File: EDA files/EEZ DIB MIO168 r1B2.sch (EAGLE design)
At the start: 295 parts, among them IC1 M24C32-WMN6P, IC10 DAC7760IPWPR, IC11 DAC7760IPWPR, IC12 OPA376AIDBVR, IC13 DAC7563TDGSR, IC14 OPA2196IDR, IC15 BTS3408G, IC16 BTS3408G, IC17 BTS3408G, IC18 BTS3408G, IC19 74HC126PW,118, IC2 Si8641BB-B-IS1, IC20 TL431B, IC21 DG468DV-T1-E3, IC22 DG468DV-T1-E3, IC23 DG468DV-T1-E3, IC24 DG468DV-T1-E3, IC25 DG468DV-T1-E3, IC26 DG468DV-T1-E3, IC27 DG468DV-T1-E3, IC28 DG468DV-T1-E3, IC29 DG468DV-T1-E3, IC3 Si8641BB-B-IS1, IC30 DG468DV-T1-E3, IC31 DG468DV-T1-E3, IC32 DG468DV-T1-E3, IC33 DG468DV-T1-E3, IC34 DG468DV-T1-E3, IC35 OPA376AIDBVR, IC36 ADS8674IDBT, IC4 L78L12, IC5 LP2985-50DBVR, IC6 LP2985-33DBVR, IC7 L79L12, IC8 STM32F446ZCT6, IC9 OPA2196IDR, J1 4907, J2 503398-1892, Q1 2N7002PS,115, Q10 BSS169, Q11 BSS169, Q12 BSS169, Q13 BSS169, Q2 2N7002PS,115, Q3 2N7002PS,115, Q4 2N7002PS,115, Q5 2N7002PS,115, Q6 BSS169, Q7 BSS169, Q8 BSS169, Q9 BSS169, X1 77317-104-28LF, X2 SSW-106-02-S-S, X3 691327310016, X4 691327310016, Y1 25MHz

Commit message: #1 fixed
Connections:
- net GND: now also IC12P.V-; no longer IC12P.V+
- net N$71: now also IC12P.V+; no longer IC12P.V-
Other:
- moved on the sheet: IC12P
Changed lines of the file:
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@@
 <setting verticaltext="up"/>
 </settings>
-<grid distance="0.1" unitdist="inch" unit="inch" style="lines" multiple="1" display="no" altdistance="0.01" altunitdist="inch" altunit="inch"/>
+<grid distance="0.025" unitdist="inch" unit="inch" style="lines" multiple="4" display="no" altdistance="0.01" altunitdist="inch" altunit="inch"/>
 <layers>
 <layer number="1" name="Top" color="4" fill="1" visible="no" active="no"/>
@@
 <layer number="111" name="111" color="7" fill="1" visible="no" active="no"/>
 <layer number="112" name="tSilk" color="7" fill="1" visible="no" active="no"/>
-<layer number="113" name="ReferenceLS" color="7" fill="1" visible="yes" active="yes"/>
-<layer number="114" name="EEZ" color="12" fill="1" visible="yes" active="yes"/>
-<layer number="115" name="CH1" color="13" fill="1" visible="yes" active="yes"/>
 <layer number="116" name="Patch_BOT" color="7" fill="1" visible="no" active="no"/>
-<layer number="117" name="CH2" color="9" fill="1" visible="yes" active="yes"/>
 <layer number="118" name="Rect_Pads" color="7" fill="1" visible="no" active="no"/>
-<layer number="119" name="CH3" color="12" fill="1" visible="yes" active="yes"/>
 <layer number="120" name="lotbs" color="7" fill="1" visible="no" active="no"/>
 <layer number="121" name="_tsilk" color="7" fill="1" visible="no" active="no"/>
@@
 <layer number="127" name="_tValues" color="7" fill="1" visible="no" active="no"/>
 <layer number="128" name="_bValues" color="7" fill="1" visible="no" active="no"/>
-<layer number="129" name="sram_cmd" color="13" fill="1" visible="yes" active="yes"/>
-<layer number="130" name="sram_ctrl" color="2" fill="1" visible="yes" active="yes"/>
 <layer number="131" name="tAdjust" color="7" fill="1" visible="no" active="no"/>
 <layer number="132" name="bAdjust" color="7" fill="1" visible="no" active="no"/>
@@
 <attribute name="VALUE" x="100.33" y="158.75" size="1.778" layer="96" rot="MR180"/>
 </instance>
-<instance part="IC12" gate="P" x="86.36" y="119.38" smashed="yes" rot="MR180">
-<attribute name="NAME" x="83.185" y="120.65" size="1.778" layer="95" rot="MR180"/>
-</instance>
 <instance part="FB4" gate="G$1" x="93.98" y="137.16" smashed="yes">
 <attribute name="NAME" x="92.075" y="138.5316" size="1.778" layer="95"/>
@@
 <attribute name="VALUE" x="121.92" y="11.938" size="1.778" layer="96"/>
 </instance>
+<instance part="IC12" gate="P" x="86.36" y="119.38" smashed="yes">
+<attribute name="NAME" x="83.185" y="118.745" size="1.778" layer="95"/>
+</instance>
 </instances>
 <busses>
@@
 </segment>
 <segment>
-<pinref part="IC12" gate="P" pin="V+"/>
 <pinref part="SUPPLY31" gate="GND" pin="GND"/>
 <wire x1="86.36" y1="109.22" x2="86.36" y2="111.76" width="0.1524" layer="91"/>
@@
 <wire x1="86.36" y1="111.76" x2="93.98" y2="111.76" width="0.1524" layer="91"/>
 <wire x1="93.98" y1="111.76" x2="93.98" y2="116.84" width="0.1524" layer="91"/>
+<pinref part="IC12" gate="P" pin="V-"/>
 <junction x="86.36" y="111.76"/>
 </segment>
@@
 <pinref part="FB4" gate="G$1" pin="1"/>
 <wire x1="88.9" y1="137.16" x2="86.36" y2="137.16" width="0.1524" layer="91"/>
-<pinref part="IC12" gate="P" pin="V-"/>
 <wire x1="86.36" y1="137.16" x2="76.2" y2="137.16" width="0.1524" layer="91"/>
 <wire x1="86.36" y1="127" x2="86.36" y2="137.16" width="0.1524" layer="91"/>
@@
 <wire x1="86.36" y1="127" x2="93.98" y2="127" width="0.1524" layer="91"/>
 <wire x1="93.98" y1="127" x2="93.98" y2="124.46" width="0.1524" layer="91"/>
+<pinref part="IC12" gate="P" pin="V+"/>
 <junction x="86.36" y="127"/>
 </segment>

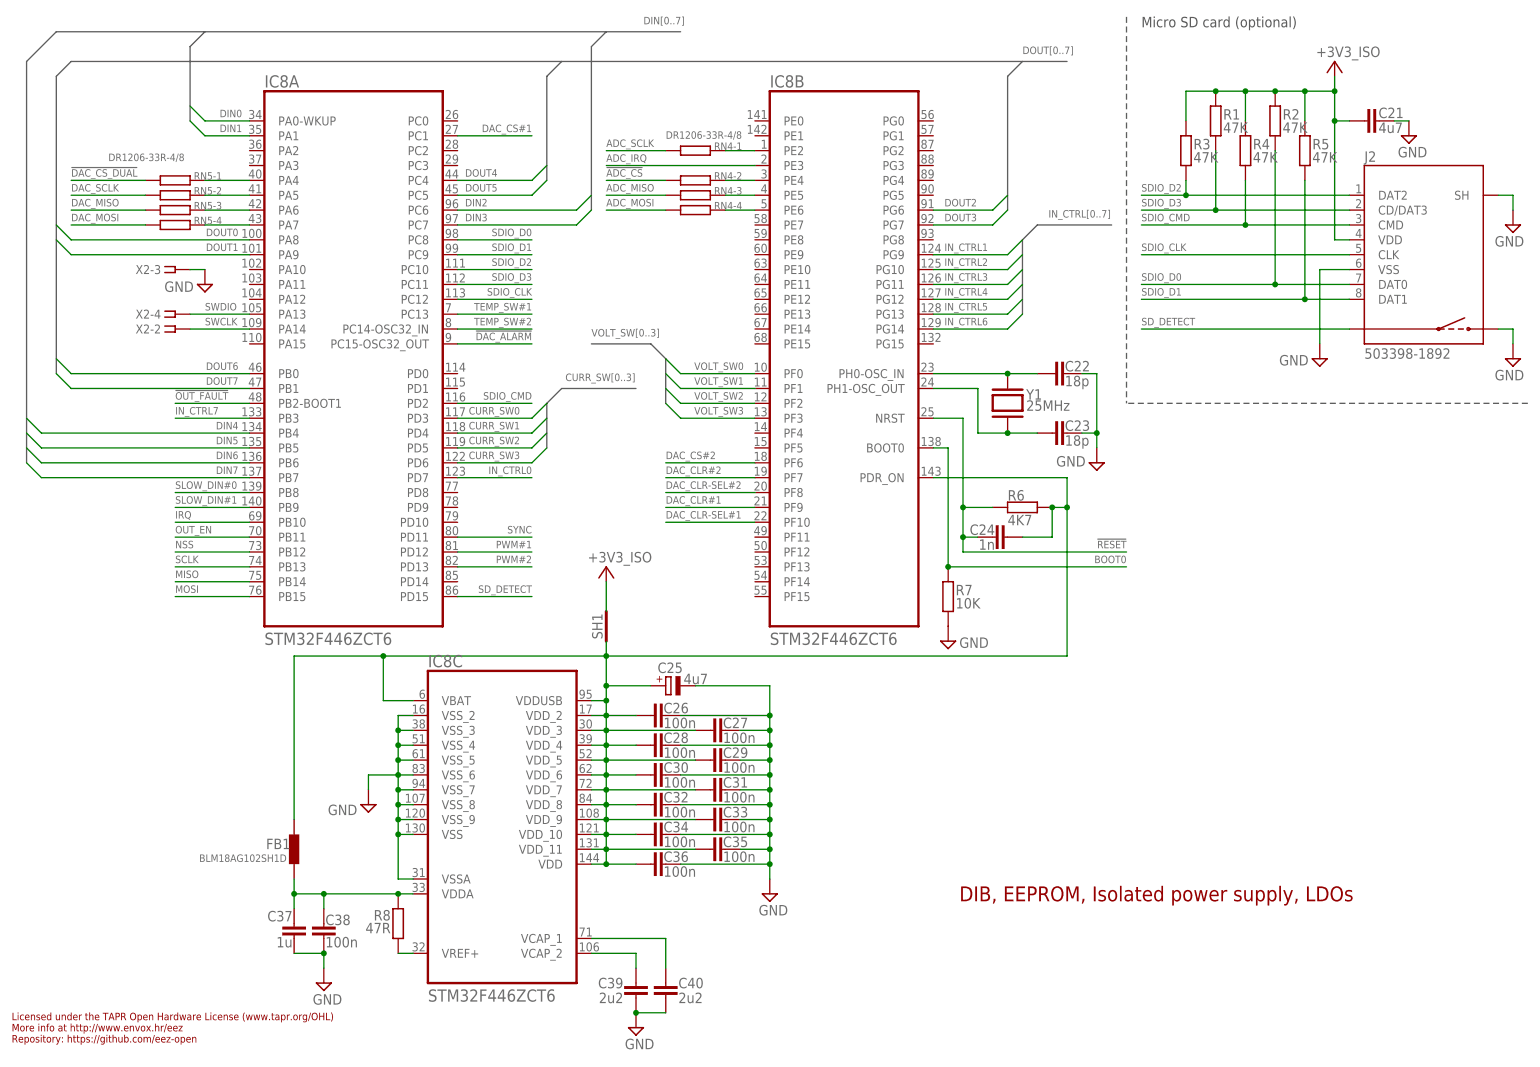
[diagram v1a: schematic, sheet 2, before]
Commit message: Slave SPI moved to SPI4
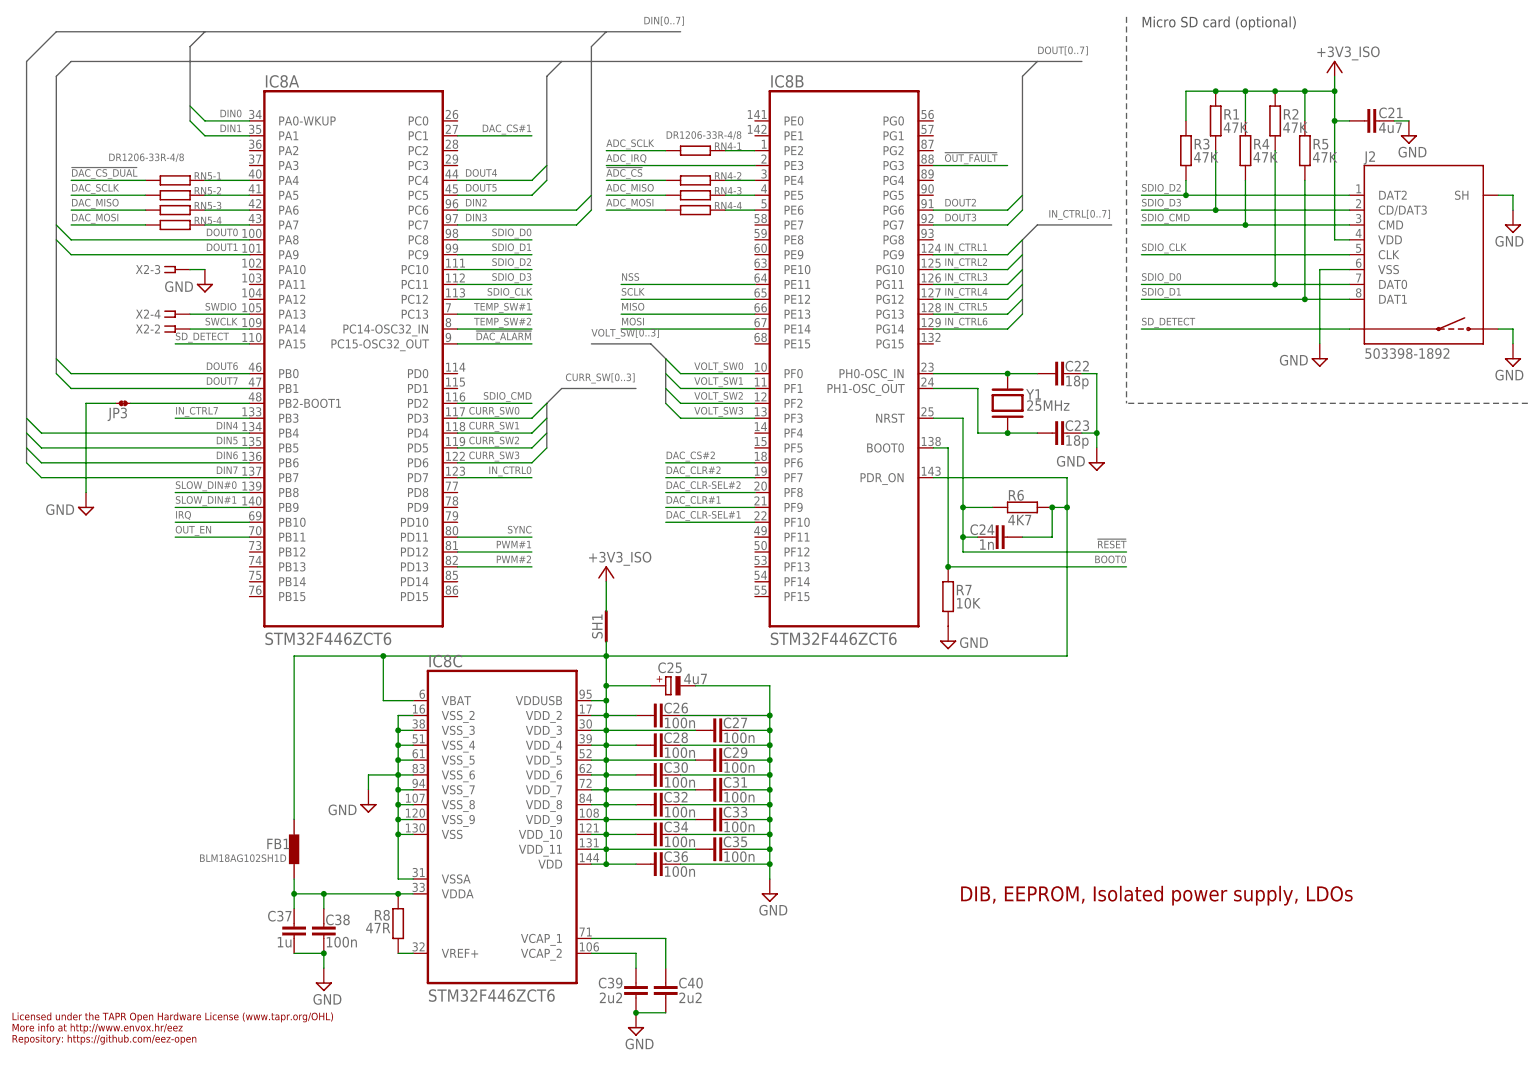
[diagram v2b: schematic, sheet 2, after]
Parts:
- added GND: (no value), EEZ_Lib1:PCB_TEST_TABSHIELD
- added JP6: JP2-CUT-0805, EEZ_Lib1:JP2-CUT-0805
- JP3: value JP3-CUT -> JP2-NOCUT-0805; device EEZ_Lib1:JP3-CUT -> EEZ_Lib1:JP2-NOCUT-0805
- JP4: value JP2-CUT-0805 -> JP3-CUT; device EEZ_Lib1:JP2-CUT-0805 -> EEZ_Lib1:JP3-CUT
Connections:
- new net N$11: IC8A.PB2-BOOT1, JP3.2
- new net N$72: IC2.B4, RN1-3.1
- net !OUT_FAULT: now also IC8B.PG3; no longer IC8A.PB2-BOOT1
- net 1V25_REF: now also JP4.NO; no longer JP3.NO
- net GND: now also GND.P$1, JP3.1
- net MISO: now also IC8B.PE13, RN1-3.2; no longer IC2.B4, IC8A.PB14
- net MOSI: now also IC8B.PE14, RN1-4.2; no longer IC8A.PB15, RN1-1.2
- net N$118: now also RN1-1.1; no longer RN1-3.1
- net N$12: now also RN1-4.1; no longer RN1-1.1
- net N$136: now also JP5.1; no longer JP4.1
- net N$137: now also JP6.1; no longer JP5.1
- net N$20: now also JP4.COM; no longer JP3.COM
- net N$28: now also JP6.2; no longer JP5.2
- net N$31: now also JP4.NC; no longer JP3.NC
- net N$87: now also JP5.2; no longer JP4.2
- net NSS: now also IC8B.PE11, RN1-1.2; no longer IC8A.PB12, RN1-3.2
- net SCLK: now also IC8B.PE12; no longer IC8A.PB13
- net SD_DETECT: now also IC8A.PA15; no longer IC8A.PD15
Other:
- moved on the sheet: JP5, RN1-1, RN1-3

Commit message: #2
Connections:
- net N$27 renamed +VSENSE2
- net N$63 renamed +VSENSE1
- net N$64 renamed -VSENSE2
- net N$79 renamed -VSENSE1
- net -12V_ISO: now also IC10.EPAD, IC11.EPAD
- net GND: no longer IC10.EPAD, IC11.EPAD
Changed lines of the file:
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@@
 </segment>
 </net>
-<net name="N$27" class="0">
+<net name="+VSENSE2" class="0">
 <segment>
 <pinref part="IC11" gate="A" pin="+VSENSE"/>
@@
 <segment>
 <pinref part="IC11" gate="A" pin="AVSS"/>
-<wire x1="116.84" y1="43.18" x2="124.46" y2="43.18" width="0.1524" layer="91"/>
+<wire x1="116.84" y1="43.18" x2="119.38" y2="43.18" width="0.1524" layer="91"/>
+<wire x1="119.38" y1="43.18" x2="124.46" y2="43.18" width="0.1524" layer="91"/>
 <wire x1="124.46" y1="43.18" x2="124.46" y2="30.48" width="0.1524" layer="91"/>
 <pinref part="C56" gate="G$1" pin="1"/>
@@
 <junction x="124.46" y="25.4"/>
 <pinref part="U$4" gate="G$1" pin="-12V_ISO"/>
+<pinref part="IC11" gate="A" pin="EPAD"/>
+<wire x1="116.84" y1="40.64" x2="119.38" y2="40.64" width="0.1524" layer="91"/>
+<wire x1="119.38" y1="40.64" x2="119.38" y2="43.18" width="0.1524" layer="91"/>
+<junction x="119.38" y="43.18"/>
 </segment>
 <segment>
@@
 <segment>
 <pinref part="IC10" gate="A" pin="AVSS"/>
-<wire x1="116.84" y1="121.92" x2="124.46" y2="121.92" width="0.1524" layer="91"/>
+<wire x1="116.84" y1="121.92" x2="119.38" y2="121.92" width="0.1524" layer="91"/>
+<wire x1="119.38" y1="121.92" x2="124.46" y2="121.92" width="0.1524" layer="91"/>
 <wire x1="124.46" y1="121.92" x2="124.46" y2="109.22" width="0.1524" layer="91"/>
 <pinref part="C46" gate="G$1" pin="1"/>
@@
 <junction x="124.46" y="104.14"/>
 <pinref part="U$11" gate="G$1" pin="-12V_ISO"/>
+<pinref part="IC10" gate="A" pin="EPAD"/>
+<wire x1="116.84" y1="119.38" x2="119.38" y2="119.38" width="0.1524" layer="91"/>
+<wire x1="119.38" y1="119.38" x2="119.38" y2="121.92" width="0.1524" layer="91"/>
+<junction x="119.38" y="121.92"/>
 </segment>
 <segment>
@@
 </segment>
 </net>
-<net name="N$64" class="0">
+<net name="-VSENSE2" class="0">
 <segment>
 <pinref part="IC11" gate="A" pin="-VSENSE"/>
@@
 </segment>
 </net>
-<net name="N$63" class="0">
+<net name="+VSENSE1" class="0">
 <segment>
 <pinref part="IC10" gate="A" pin="+VSENSE"/>
@@
 </segment>
 </net>
-<net name="N$79" class="0">
+<net name="-VSENSE1" class="0">
 <segment>
 <pinref part="IC10" gate="A" pin="-VSENSE"/>
@@
 </segment>
 <segment>
-<pinref part="IC11" gate="A" pin="EPAD"/>
-<wire x1="86.36" y1="43.18" x2="81.28" y2="43.18" width="0.1524" layer="91"/>
-<wire x1="81.28" y1="43.18" x2="81.28" y2="40.64" width="0.1524" layer="91"/>
 <pinref part="IC11" gate="A" pin="GND"/>
 <wire x1="81.28" y1="40.64" x2="81.28" y2="38.1" width="0.1524" layer="91"/>
 <wire x1="86.36" y1="45.72" x2="81.28" y2="45.72" width="0.1524" layer="91"/>
-<wire x1="81.28" y1="45.72" x2="81.28" y2="43.18" width="0.1524" layer="91"/>
-<junction x="81.28" y="43.18"/>
+<wire x1="81.28" y1="45.72" x2="81.28" y2="40.64" width="0.1524" layer="91"/>
 <pinref part="IC11" gate="A" pin="DVDD-EN"/>
 <wire x1="86.36" y1="50.8" x2="81.28" y2="50.8" width="0.1524" layer="91"/>
@@
 </segment>
 <segment>
-<pinref part="IC10" gate="A" pin="EPAD"/>
-<wire x1="86.36" y1="121.92" x2="81.28" y2="121.92" width="0.1524" layer="91"/>
-<wire x1="81.28" y1="121.92" x2="81.28" y2="119.38" width="0.1524" layer="91"/>
 <pinref part="IC10" gate="A" pin="GND"/>
 <wire x1="81.28" y1="119.38" x2="81.28" y2="116.84" width="0.1524" layer="91"/>
 <wire x1="86.36" y1="124.46" x2="81.28" y2="124.46" width="0.1524" layer="91"/>
-<wire x1="81.28" y1="124.46" x2="81.28" y2="121.92" width="0.1524" layer="91"/>
-<junction x="81.28" y="121.92"/>
+<wire x1="81.28" y1="124.46" x2="81.28" y2="119.38" width="0.1524" layer="91"/>
 <pinref part="IC10" gate="A" pin="DVDD-EN"/>
 <wire x1="86.36" y1="129.54" x2="81.28" y2="129.54" width="0.1524" layer="91"/>

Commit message: #3
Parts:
- removed JP6: JP2-CUT-0805, EEZ_Lib1:JP2-CUT-0805
- C21: value 4u7 -> N.C.
- J2: value 503398-1892 -> N.C.
- JP3: value JP2-NOCUT-0805 -> JP3-CUT; device EEZ_Lib1:JP2-NOCUT-0805 -> EEZ_Lib1:JP3-CUT
- JP4: value JP3-CUT -> JP2-CUT-0805; device EEZ_Lib1:JP3-CUT -> EEZ_Lib1:JP2-CUT-0805
- R1, R2, R3, R4, R5: value 47K -> N.C.
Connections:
- removed net N$11: IC8A.PB2-BOOT1, JP3.2
- removed net N$39: IC8B.PE2, RN4-1.2
- removed net N$40: IC8B.PE4, RN4-2.2
- removed net N$41: IC8B.PE5, RN4-3.2
- removed net N$44: IC8B.PE6, RN4-4.2
- new net N$27: IC8A.PB14, RN5-3.2
- new net N$29: IC8A.PB15, RN5-4.2
- new net N$34: IC8A.PB12, RN5-1.2
- new net N$37: IC8A.PB13, RN5-2.2
- net !ADC_CS: now also RN5-1.1; no longer RN4-2.1
- net !DAC_CS_DUAL: now also RN4-1.1; no longer RN5-1.1
- net 1V25_REF: now also JP3.NO; no longer JP4.NO
- net ADC_IRQ: now also IC8A.PD8; no longer IC8B.PE3
- net ADC_MISO: now also RN5-3.1; no longer RN4-3.1
- net ADC_MOSI: now also RN5-4.1; no longer RN4-4.1
- net ADC_SCLK: now also RN5-2.1; no longer RN4-1.1
- net DAC_MISO: now also RN4-3.1; no longer RN5-3.1
- net DAC_MOSI: now also RN4-4.1; no longer RN5-4.1
- net DAC_SCLK: now also RN4-2.1; no longer RN5-2.1
- net GND: now also IC8A.PB2-BOOT1; no longer JP3.1
- net N$100: now also RN4-3.2; no longer RN5-3.2
- net N$103: now also RN4-4.2; no longer RN5-4.2
- net N$136: now also JP4.1; no longer JP5.1
- net N$137: now also JP5.1; no longer JP6.1
- net N$20: now also JP3.COM; no longer JP4.COM
- net N$28: now also JP5.2; no longer JP6.2
- net N$31: now also JP3.NC; no longer JP4.NC
- net N$81: now also RN4-1.2; no longer RN5-1.2
- net N$87: now also JP4.2; no longer JP5.2
- net N$98: now also RN4-2.2; no longer RN5-2.2
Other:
- moved on the sheet: JP5, RN4-1, RN4-2, RN4-3, RN4-4, RN5-1, RN5-2, RN5-3, RN5-4
